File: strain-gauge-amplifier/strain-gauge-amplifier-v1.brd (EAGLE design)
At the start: 49.8 x 40.3 mm, 25 parts, among them IC2 INA125U, M1 #4-BARE_MOUNTING_HOLE/.300, M2 #4-BARE_MOUNTING_HOLE/.300, M3 #4-BARE_MOUNTING_HOLE/.300, M4 #4-BARE_MOUNTING_HOLE/.300, Q1 PMV45EN

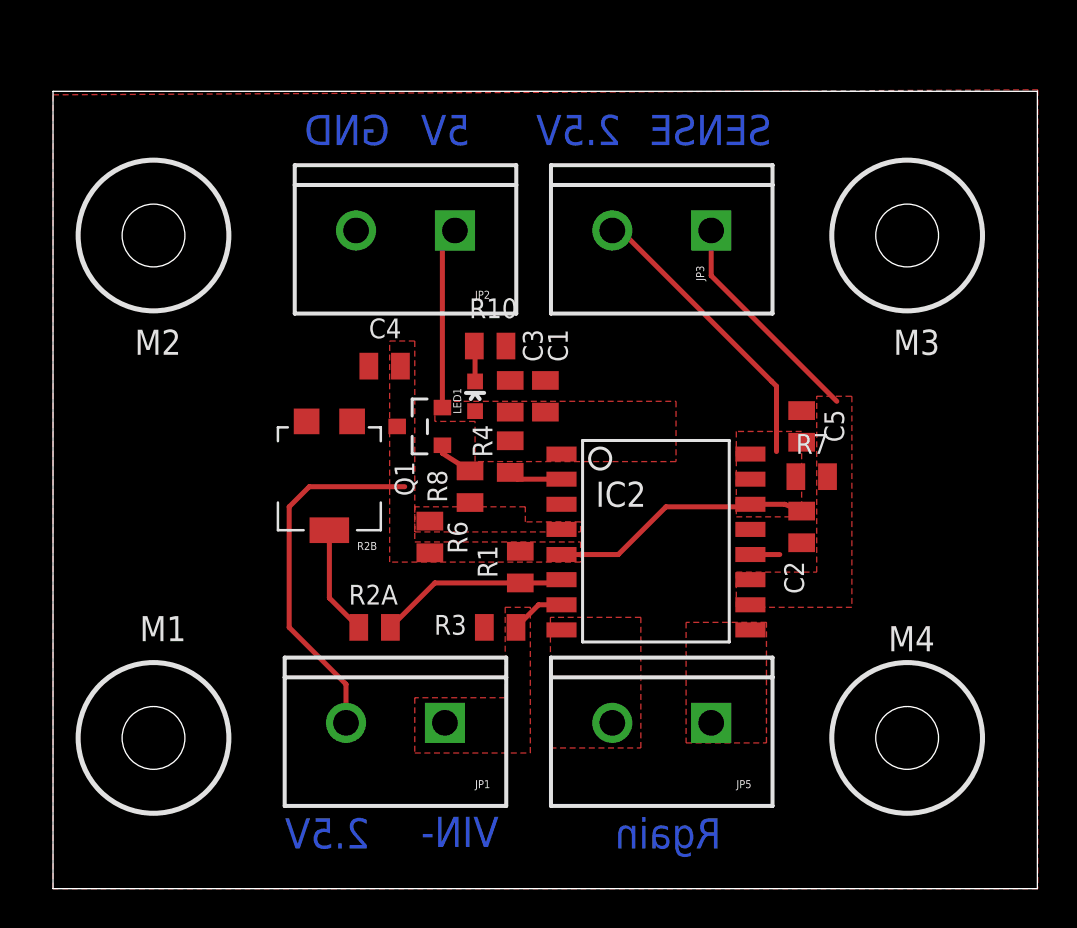
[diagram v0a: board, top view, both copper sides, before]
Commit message: Cleaned up board a bit - mostly made things wider, cleaned up one part placement.
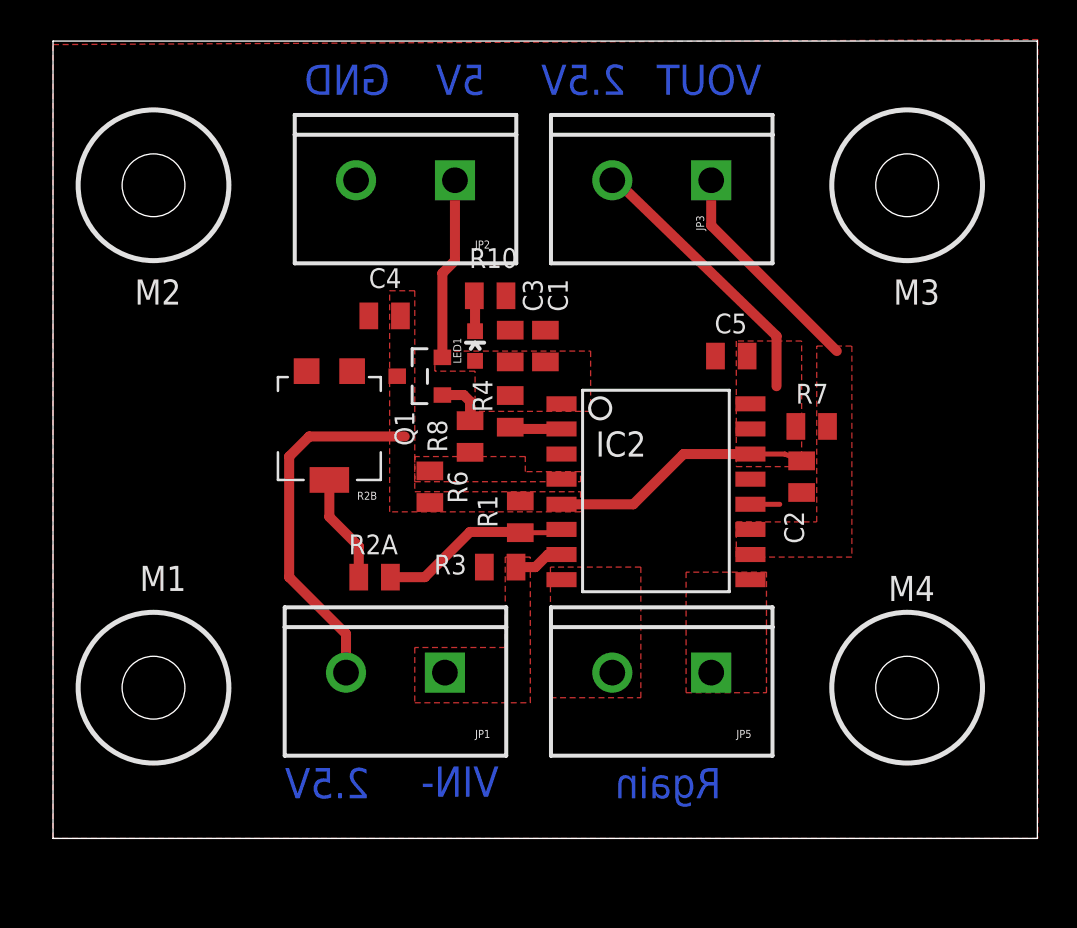
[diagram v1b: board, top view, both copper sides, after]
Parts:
- moved C5 5.03 mm to (34.3, 24.4), turned to 180 degrees
- moved R3 3.05 mm to (22.6, 13.7)
- moved M2 2.54 mm to (5.08, 33.0)
- moved M3 2.54 mm to (43.2, 33.0)
- moved C2 2.54 mm to (37.8, 18.3)
- moved R1 2.54 mm to (23.6, 16.3)
- moved R2A 2.54 mm to (16.3, 13.2)
- moved R6 2.54 mm to (19.1, 17.8)
- moved JP1 2.54 mm to (19.8, 8.38)
- moved JP5 2.54 mm to (33.3, 8.38)
- moved M1 2.54 mm to (5.08, 7.62)
- moved M4 2.54 mm to (43.2, 7.62)
- moved C1 2.54 mm to (24.9, 24.9)
- moved C3 2.54 mm to (23.1, 24.9)
- moved C4 2.54 mm to (16.8, 26.4)
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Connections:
- net SENSE renamed VOUT
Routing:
- net 2.5VREF: track 46.5 -> 45.7 mm
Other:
- board text added: "VOUT"
- board text removed: "SENSE"

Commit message: Changed trim pot footprint; had to change layout.
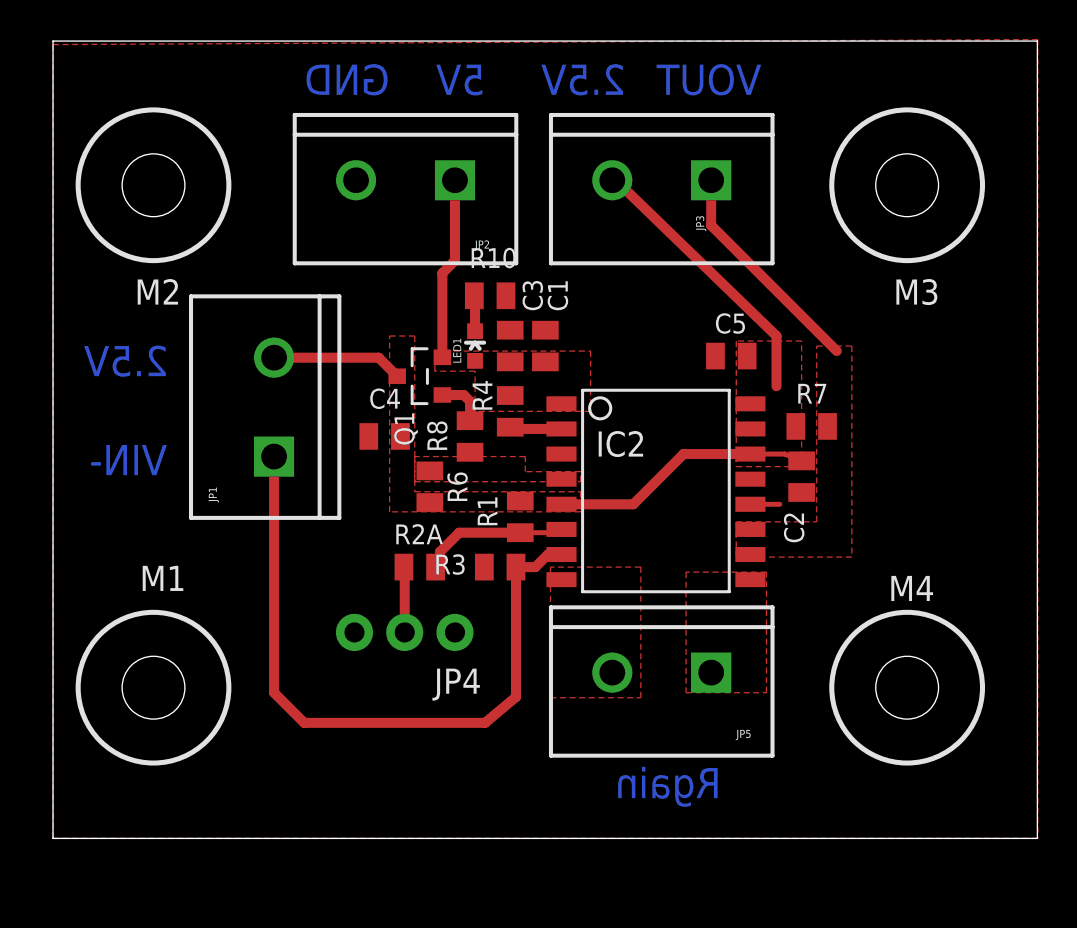
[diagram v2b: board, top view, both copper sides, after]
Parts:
- removed R2B: 50ohm/20turn, SparkFun-Electromechanical:TRIMPOT-5MM
- added JP4: 50ohm/20turn, SparkFun-Connectors:1X03_NO_SILK
- moved JP1 13.9 mm to (11.2, 19.3), turned to 90 degrees
- moved C4 6.10 mm to (16.8, 20.3)
- moved R2A 2.34 mm to (18.5, 13.7)
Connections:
- net GND: now also JP4.3; no longer R2B.C
- net N$1: now also JP4.2; no longer R2B.B
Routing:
- net VIN-: track 2.56 -> 34.4 mm
- net 2.5VREF: track 45.7 -> 33.9 mm
- net N$1: track 5.53 -> 3.32 mm
- net VIN+: track 9.68 -> 7.47 mm
- removed copper zone on layer 1, net VIN-
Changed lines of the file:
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@@
 <?xml version="1.0" encoding="utf-8"?>
 <!DOCTYPE eagle SYSTEM "eagle.dtd">
-<eagle version="6.5.0">
+<eagle version="6.4">
 <drawing>
 <settings>
@@
 <text x="21.844" y="37.592" size="1.524" layer="16" font="vector" ratio="20" rot="SMR0">5V</text>
 <text x="17.018" y="37.592" size="1.524" layer="16" font="vector" ratio="20" rot="SMR0">GND</text>
-<text x="22.5298" y="2.1082" size="1.524" layer="16" font="vector" ratio="20" rot="SMR0">VIN-</text>
-<text x="16.002" y="2.032" size="1.524" layer="16" font="vector" ratio="20" rot="SMR0">2.5V</text>
+<text x="5.7658" y="18.3642" size="1.524" layer="16" font="vector" ratio="20" rot="SMR0">VIN-</text>
+<text x="5.842" y="23.368" size="1.524" layer="16" font="vector" ratio="20" rot="SMR0">2.5V</text>
 <text x="33.782" y="2.032" size="1.524" layer="16" font="vector" ratio="20" rot="SMR0">Rgain</text>
 </plain>
@@
 <attribute name="VALUE" x="25.014" y="24.092" size="1" layer="27" ratio="10" rot="R90"/>
 </element>
-<element name="JP1" library="SparkFun-Connectors" package="SCREWTERMINAL-5MM-2" value="STRAIN" x="19.812" y="8.382" smashed="yes" rot="R180">
-<attribute name="NAME" x="21.336" y="5.08" size="0.4064" layer="25"/>
-<attribute name="VALUE" x="21.082" y="7.112" size="0.4064" layer="27" rot="R180"/>
+<element name="JP1" library="SparkFun-Connectors" package="SCREWTERMINAL-5MM-2" value="STRAIN" x="11.176" y="19.304" smashed="yes" rot="R90">
+<attribute name="NAME" x="7.874" y="17.78" size="0.4064" layer="25" rot="R270"/>
+<attribute name="VALUE" x="9.906" y="18.034" size="0.4064" layer="27" rot="R90"/>
 </element>
 <element name="JP2" library="SparkFun-Connectors" package="SCREWTERMINAL-5MM-2" value="" x="20.32" y="33.274" smashed="yes" rot="R180">
@@
 <attribute name="VALUE" x="25.522" y="15.456" size="1" layer="27" ratio="10" rot="R90"/>
 </element>
-<element name="R2A" library="rcl_custom" package="0805-C-NOSILK" value="100" x="16.256" y="13.208" smashed="yes">
-<attribute name="NAME" x="14.948" y="14.362" size="1" layer="25" ratio="10"/>
-<attribute name="VALUE" x="15.456" y="11.308" size="1" layer="27" ratio="10"/>
+<element name="R2A" library="rcl_custom" package="0805-C-NOSILK" value="100" x="18.542" y="13.716" smashed="yes">
+<attribute name="NAME" x="17.234" y="14.87" size="1" layer="25" ratio="10"/>
+<attribute name="VALUE" x="17.742" y="11.816" size="1" layer="27" ratio="10"/>
 </element>
 <element name="R7" library="rcl_custom" package="0805-C-NOSILK" value="NP (10k)" x="38.354" y="20.828" smashed="yes">
@@
 <attribute name="VALUE" x="22.982" y="19.52" size="1" layer="27" ratio="10" rot="R90"/>
 </element>
-<element name="R2B" library="SparkFun-Electromechanical" package="TRIMPOT-5MM" value="50ohm/20turn" x="13.97" y="21.082" smashed="yes" rot="R180">
-<attribute name="NAME" x="16.383" y="17.526" size="0.4064" layer="25" rot="R180"/>
-<attribute name="VALUE" x="16.129" y="21.082" size="0.4064" layer="27" rot="R180"/>
-</element>
 <element name="LED1" library="SparkFun-LED" package="LED-0603" value="2.1V/20mA" x="21.336" y="24.892" smashed="yes">
 <attribute name="NAME" x="20.6375" y="24.003" size="0.4064" layer="25" rot="R90"/>
@@
 <attribute name="VALUE" x="35.946" y="19.088" size="1" layer="27" ratio="10" rot="R270"/>
 </element>
-<element name="C4" library="rcl_custom" package="0805-C-NOSILK" value="100n" x="16.764" y="26.416" smashed="yes" rot="R180">
-<attribute name="NAME" x="15.964" y="27.824" size="1" layer="25" ratio="10"/>
-<attribute name="VALUE" x="17.564" y="28.316" size="1" layer="27" ratio="10" rot="R180"/>
+<element name="C4" library="rcl_custom" package="0805-C-NOSILK" value="100n" x="16.764" y="20.32" smashed="yes" rot="R180">
+<attribute name="NAME" x="15.964" y="21.728" size="1" layer="25" ratio="10"/>
+<attribute name="VALUE" x="17.564" y="22.22" size="1" layer="27" ratio="10" rot="R180"/>
 </element>
 <element name="C5" library="rcl_custom" package="0805-C-NOSILK" value="100n" x="34.29" y="24.384" smashed="yes" rot="R180">
@@
 <attribute name="VALUE" x="46.355" y="4.445" size="1.27" layer="27"/>
 </element>
+<element name="JP4" library="SparkFun-Connectors" package="1X03_NO_SILK" value="50ohm/20turn" x="20.32" y="10.414" rot="R180"/>
 </elements>
 <signals>
@@
 <contactref element="R3" pad="2"/>
 <contactref element="IC2" pad="7"/>
-<polygon width="0.254" layer="1">
-<vertex x="18.288" y="6.858"/>
-<vertex x="24.13" y="6.858"/>
-<vertex x="24.13" y="14.224"/>
-<vertex x="22.86" y="14.224"/>
-<vertex x="22.86" y="9.652"/>
-<vertex x="18.288" y="9.652"/>
-</polygon>
 <wire x1="25.7048" y1="14.351" x2="25.019" y2="14.351" width="0.508" layer="1"/>
 <wire x1="25.019" y1="14.351" x2="24.384" y2="13.716" width="0.508" layer="1"/>
 <wire x1="24.384" y1="13.716" x2="23.406" y2="13.716" width="0.508" layer="1"/>
+<wire x1="23.406" y1="13.716" x2="23.406" y2="7.15" width="0.508" layer="1"/>
+<wire x1="23.406" y1="7.15" x2="21.844" y2="5.842" width="0.508" layer="1"/>
+<wire x1="21.844" y1="5.842" x2="12.7" y2="5.842" width="0.508" layer="1"/>
+<wire x1="12.7" y1="5.842" x2="11.176" y2="7.366" width="0.508" layer="1"/>
+<wire x1="11.176" y1="7.366" x2="11.176" y2="19.304" width="0.508" layer="1"/>
 </signal>
 <signal name="VIN+">
@@
 <wire x1="23.622" y1="15.456" x2="25.5398" y2="15.456" width="0.254" layer="1"/>
 <wire x1="25.5398" y1="15.456" x2="25.7048" y2="15.621" width="0.254" layer="1"/>
-<wire x1="17.056" y1="13.208" x2="18.796" y2="13.208" width="0.508" layer="1"/>
-<wire x1="18.796" y1="13.208" x2="21.082" y2="15.494" width="0.508" layer="1"/>
-<wire x1="21.082" y1="15.494" x2="23.584" y2="15.494" width="0.508" layer="1"/>
-<wire x1="23.584" y1="15.494" x2="23.622" y2="15.456" width="0.508" layer="1"/>
+<wire x1="23.622" y1="15.456" x2="20.536" y2="15.456" width="0.508" layer="1"/>
+<wire x1="20.536" y1="15.456" x2="19.558" y2="14.478" width="0.508" layer="1"/>
+<wire x1="19.558" y1="14.478" x2="19.558" y2="13.932" width="0.508" layer="1"/>
+<wire x1="19.558" y1="13.932" x2="19.342" y2="13.716" width="0.508" layer="1"/>
 </signal>
 <signal name="GND">
@@
 <contactref element="R10" pad="1"/>
 <contactref element="R3" pad="1"/>
-<contactref element="R2B" pad="C"/>
 <contactref element="C2" pad="2"/>
 <contactref element="C4" pad="2"/>
@@
 </polygon>
 <wire x1="35.2552" y1="16.891" x2="36.741" y2="16.891" width="0.254" layer="1"/>
+<contactref element="JP4" pad="3"/>
 </signal>
 <signal name="N$3">
@@
 <vertex x="26.67" y="16.51"/>
 <vertex x="17.018" y="16.51"/>
-<vertex x="17.018" y="27.686"/>
-<vertex x="18.288" y="27.686"/>
+<vertex x="17.018" y="25.4"/>
+<vertex x="18.288" y="25.4"/>
 <vertex x="18.288" y="17.526"/>
 <vertex x="26.67" y="17.526"/>
 </polygon>
-<wire x1="14.812" y1="8.382" x2="14.812" y2="10.334" width="0.508" layer="1"/>
-<wire x1="14.812" y1="10.334" x2="11.938" y2="13.208" width="0.508" layer="1"/>
-<wire x1="11.938" y1="13.208" x2="11.938" y2="19.304" width="0.508" layer="1"/>
-<wire x1="11.938" y1="19.304" x2="12.954" y2="20.32" width="0.508" layer="1"/>
-<wire x1="12.954" y1="20.32" x2="17.78" y2="20.32" width="0.508" layer="1"/>
 <polygon width="0.254" layer="1" rank="2">
 <vertex x="34.544" y="18.796"/>
@@
 <wire x1="28.448" y1="33.274" x2="36.576" y2="25.4" width="0.508" layer="1"/>
 <wire x1="36.576" y1="25.4" x2="36.576" y2="22.86" width="0.508" layer="1"/>
+<wire x1="11.176" y1="24.304" x2="16.463" y2="24.304" width="0.508" layer="1"/>
+<wire x1="16.463" y1="24.304" x2="17.399" y2="23.368" width="0.508" layer="1"/>
 </signal>
 <signal name="VREFOUT">
@@
 <signal name="N$1">
 <contactref element="R2A" pad="1"/>
-<contactref element="R2B" pad="B"/>
-<wire x1="15.456" y1="13.208" x2="15.456" y2="14.77" width="0.508" layer="1"/>
-<wire x1="15.456" y1="14.77" x2="13.97" y2="16.256" width="0.508" layer="1"/>
-<wire x1="13.97" y1="16.256" x2="13.97" y2="18.122" width="0.508" layer="1"/>
+<contactref element="JP4" pad="2"/>
+<wire x1="17.78" y1="10.414" x2="17.78" y2="13.678" width="0.508" layer="1"/>
+<wire x1="17.78" y1="13.678" x2="17.742" y2="13.716" width="0.508" layer="1"/>
 </signal>
 <signal name="VOUT">
